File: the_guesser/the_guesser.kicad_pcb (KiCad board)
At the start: 4 copper layers, 24 x 75 mm, 96 parts, among them J1 Screw_Terminal_01x06, J2 Conn_Coaxial, J3 BMI-S-209-F, J4 Screw_Terminal_01x06, J6 BMI-S-209-F, J7 USB_C_Receptacle_USB2.0_16P, Q1 AS2312, Q2 AS2312, Q3 AS2312, Q4 AS2312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

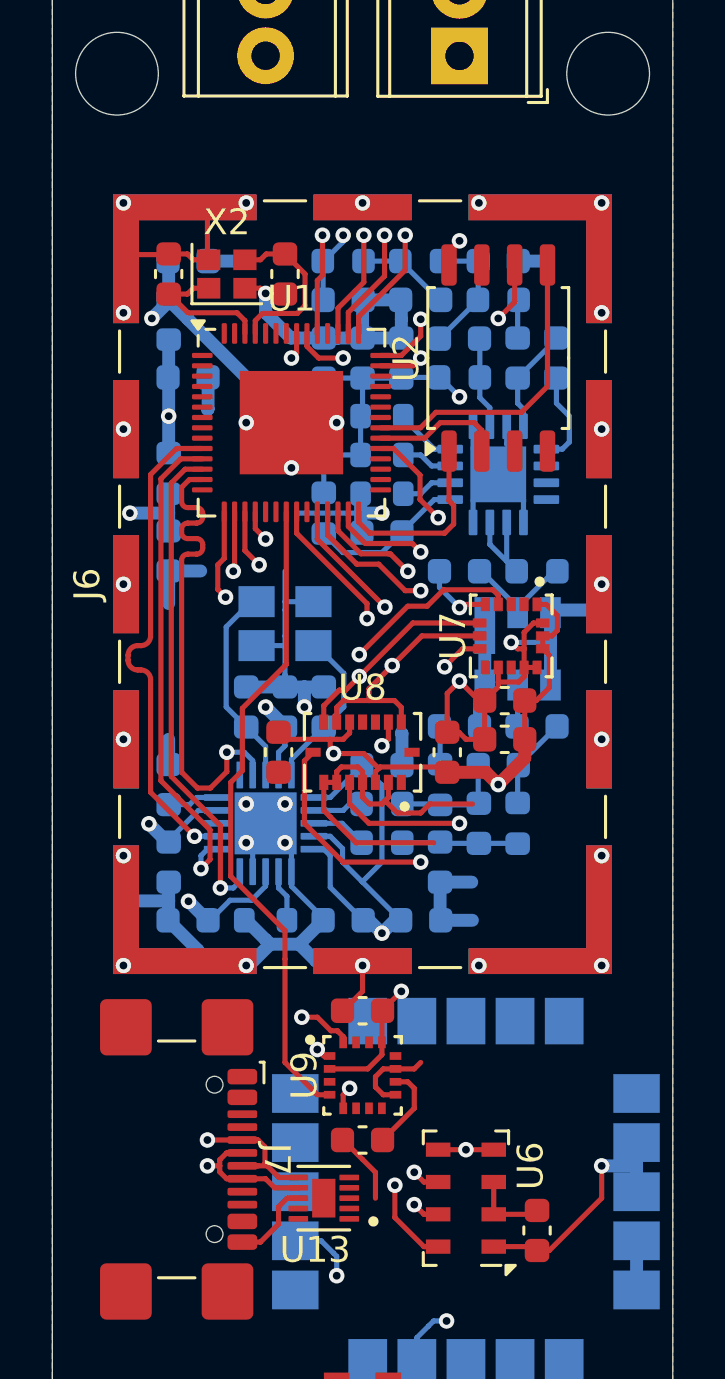
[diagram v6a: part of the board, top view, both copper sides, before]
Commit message: Finished routing Guesser
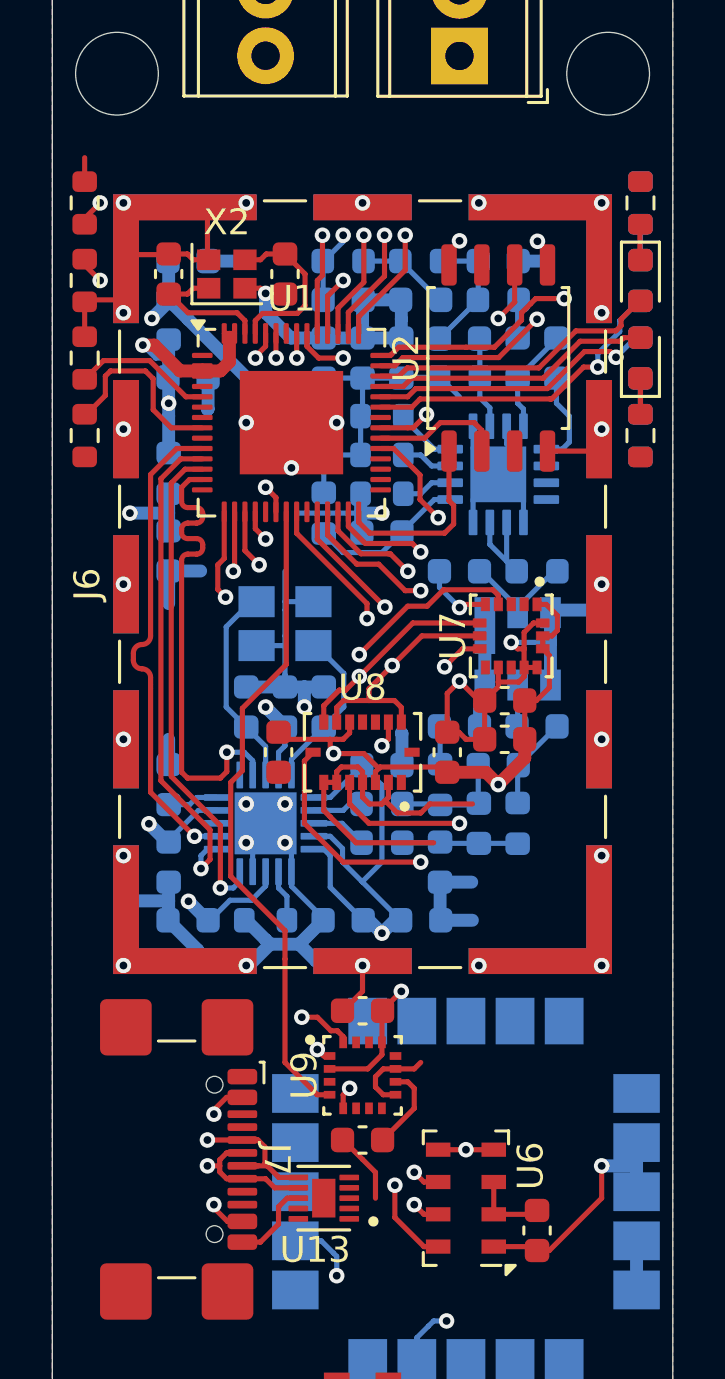
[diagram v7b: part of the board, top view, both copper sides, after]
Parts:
- added D2: LED, LED_SMD:LED_0603_1608Metric, F.Cu at (222.8, 48.5)
- added D3: LED, LED_SMD:LED_0603_1608Metric, F.Cu at (222.8, 51.5)
- added D4: LED, LED_SMD:LED_0603_1608Metric, B.Cu at (222.8, 48.5)
- added D5: LED, LED_SMD:LED_0603_1608Metric, B.Cu at (222.8, 51.5)
- added R10: 10k, Resistor_SMD:R_0603_1608Metric, F.Cu at (201.2, 51.5)
- added R11: 10k, Resistor_SMD:R_0603_1608Metric, F.Cu at (201.2, 54.5)
- added R12: 10k, Resistor_SMD:R_0603_1608Metric, F.Cu at (201.2, 48.5)
- added R13: 10k, Resistor_SMD:R_0603_1608Metric, F.Cu at (201.2, 45.5)
- added R14: 1k, Resistor_SMD:R_0603_1608Metric, F.Cu at (222.8, 45.5)
- added R15: 1k, Resistor_SMD:R_0603_1608Metric, F.Cu at (222.8, 54.5)
- added R16: 1k, Resistor_SMD:R_0603_1608Metric, B.Cu at (222.8, 45.5)
- added R17: 1k, Resistor_SMD:R_0603_1608Metric, B.Cu at (222.8, 54.5)
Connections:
- net Net-(J2-In) renamed /Transmitter/RF_OUT
- J7 pad A4: V_{USB} -> VCC
- J7 pad A9: V_{USB} -> VCC
- J7 pad B4: V_{USB} -> VCC
- J7 pad B9: V_{USB} -> VCC
- U1 pad 2: Net-(U1-VDD3P3-Pad2) -> VCC
- U1 pad 20: unconnected-(U1-VDD3P3_RTC-Pad20) -> VCC
- U1 pad 3: Net-(U1-VDD3P3-Pad2) -> VCC
- U1 pad 37: unconnected-(U1-SPICLK_P-Pad37) -> LED3
- U1 pad 38: unconnected-(U1-GPIO33-Pad38) -> LED4
- U1 pad 39: unconnected-(U1-GPIO34-Pad39) -> LED2
- U1 pad 40: unconnected-(U1-GPIO35-Pad40) -> LED1
- U1 pad 46: unconnected-(U1-VDD3P3_CPU-Pad46) -> VCC
- U1 pad 5: unconnected-(U1-GPIO0-Pad5) -> Net-(U1-GPIO0)
- U1 pad 51: unconnected-(U1-GPIO45-Pad51) -> Net-(U1-GPIO45)
- U1 pad 52: unconnected-(U1-GPIO46-Pad52) -> Net-(U1-GPIO46)
- U1 pad 55: Net-(U1-VDDA-Pad55) -> VCC
- U1 pad 56: Net-(U1-VDDA-Pad55) -> VCC
- U1 pad 8: unconnected-(U1-GPIO3-Pad8) -> Net-(U1-GPIO3)
- U4 pad 6: HGM -> unconnected-(U4-HGM-Pad6)
- U4 pad 7: LNA_EN -> unconnected-(U4-LNA-EN-Pad7)
- U4 pad 8: PA_EN -> unconnected-(U4-PA-EN-Pad8)
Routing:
- net GND: track 134.8 -> 179.7 mm
- net VCC: track 49.1 -> 62.5 mm, vias 8 -> 13
- net Net-(U1-GPIO45): track 0.00 -> 12.8 mm, vias 0 -> 2
- net LED3: track 0.00 -> 12.3 mm, vias 0 -> 1
- net LED1: track 0.00 -> 11.4 mm
- net LED4: track 0.00 -> 11.2 mm, vias 0 -> 1
- net LED2: track 0.00 -> 10.8 mm
- net Net-(U1-GPIO46): track 0.00 -> 10.3 mm, vias 0 -> 2
- net Net-(U1-GPIO3): track 0.00 -> 7.30 mm
- net Net-(U1-GPIO0): track 0.00 -> 5.43 mm
- net SDA1: track 54.9 -> 57.7 mm
- net VCC_{CC1190}: track 38.1 -> 36.0 mm, vias 2 -> 1
- net Net-(D2-K): track 0.00 -> 1.42 mm
- net Net-(D5-K): track 0.00 -> 1.39 mm
- net Net-(D4-K): track 0.00 -> 1.39 mm
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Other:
- board text added: "24.0000 mm x 75.0000 mm"
- board text removed: "156.1423 mm x 73.8183 mm"

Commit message: Started Timer Programmer
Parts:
- removed J7: USB_C_Receptacle_USB2.0_16P, Connector_USB:USB_C_Receptacle_GCT_USB4110
- added J5: R41-B583A, locals_but_working_PLEASE:CONN_R41-B583A_MIT, F.Cu at (203.6, 82.5)
- moved U13 1.03 mm to (211.5, 84.2), turned to -90 degrees
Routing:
- net GND: track 179.7 -> 186.5 mm
- net USB_D-: track 58.6 -> 62.2 mm, vias 2 -> 3
- net USB_D+: track 57.8 -> 60.9 mm, vias 2 -> 3
- net VCC: track 62.5 -> 65.1 mm
